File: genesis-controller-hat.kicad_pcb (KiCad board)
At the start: 2 copper layers, 65 x 56 mm, 5 parts, among them J1 GPIO, J2 DSUB-9_Socket_Horizontal_P2.7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, J3 DSUB-9_Socket_Horizontal_P2.7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

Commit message: Fix lib_footprint_mismatch -- DRC down to a single pre-existing item
J1's embedded PinSocket_2x20_P2.54mm_Vertical footprint drifted from the
system library's copy during the KiCad 9->10 upgrade (pad shape changed
from OVAL to CIRCLE -- cosmetic for a 1.7x1.7mm round pad, since equal
width/height makes the two shapes identical). Fixed the same way as the
schematic-side symbol drift: removed J1, added a fresh copy of the same
footprint straight from the system library at the same position/rotation/
flip state, and reassigned every pad's net by pad number. Verified pad
count, positions, sizes, and drills matched exactly before swapping (only
shape differed).

Side effect: unconnected_items dropped from 2 to 1. Removing J1 pruned
several stale net-table entries for GPIO pins with no real circuit (I2C,
UART, I2S, EEPROM ID -- already inert, unreferenced by any track), which
happened to include the "J1 pins 2/4 unused +5V" pair. The remaining
+3.3V pins 1/17 item is unrelated and not fixable without a pointless
jumper (they're already tied together upstream on the Pi).

DRC: 2 errors/1 warning -> 1 error/0 warnings. ERC remains 0/0.
check_pinmap.py and a top+bottom render confirm nothing else moved.

Co-Authored-By: Claude Sonnet 5 <noreply@anthropic.com>
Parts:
- J1: value GPIO -> PinSocket_2x20_P2.54mm_Vertical; footprint Connector_PinSocket_2.54mm:PinSocket_2x20_P2.54mm_Vertical -> PinSocket_2x20_P2.54mm_Vertical
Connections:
- J1 pad 10: /GPIO15/RXD0 -> (no net)
- J1 pad 12: /GPIO18/PCM.CLK -> (no net)
- J1 pad 2: +5V -> (no net)
- J1 pad 21: /GPIO9/SPI0.MISO -> (no net)
- J1 pad 22: /GPIO25 -> (no net)
- J1 pad 23: /GPIO11/SPI0.SCLK -> (no net)
- J1 pad 24: /GPIO8/SPI0.CE0 -> (no net)
- J1 pad 27: /ID_SDA -> (no net)
- J1 pad 28: /ID_SCL -> (no net)
- J1 pad 3: /GPIO2/SDA1 -> (no net)
- J1 pad 35: /GPIO19/PCM.FS -> (no net)
- J1 pad 38: /GPIO20/PCM.DIN -> (no net)
- J1 pad 4: +5V -> (no net)
- J1 pad 40: /GPIO21/PCM.DOUT -> (no net)
- J1 pad 5: /GPIO3/SCL1 -> (no net)
- J1 pad 8: /GPIO14/TXD0 -> (no net)

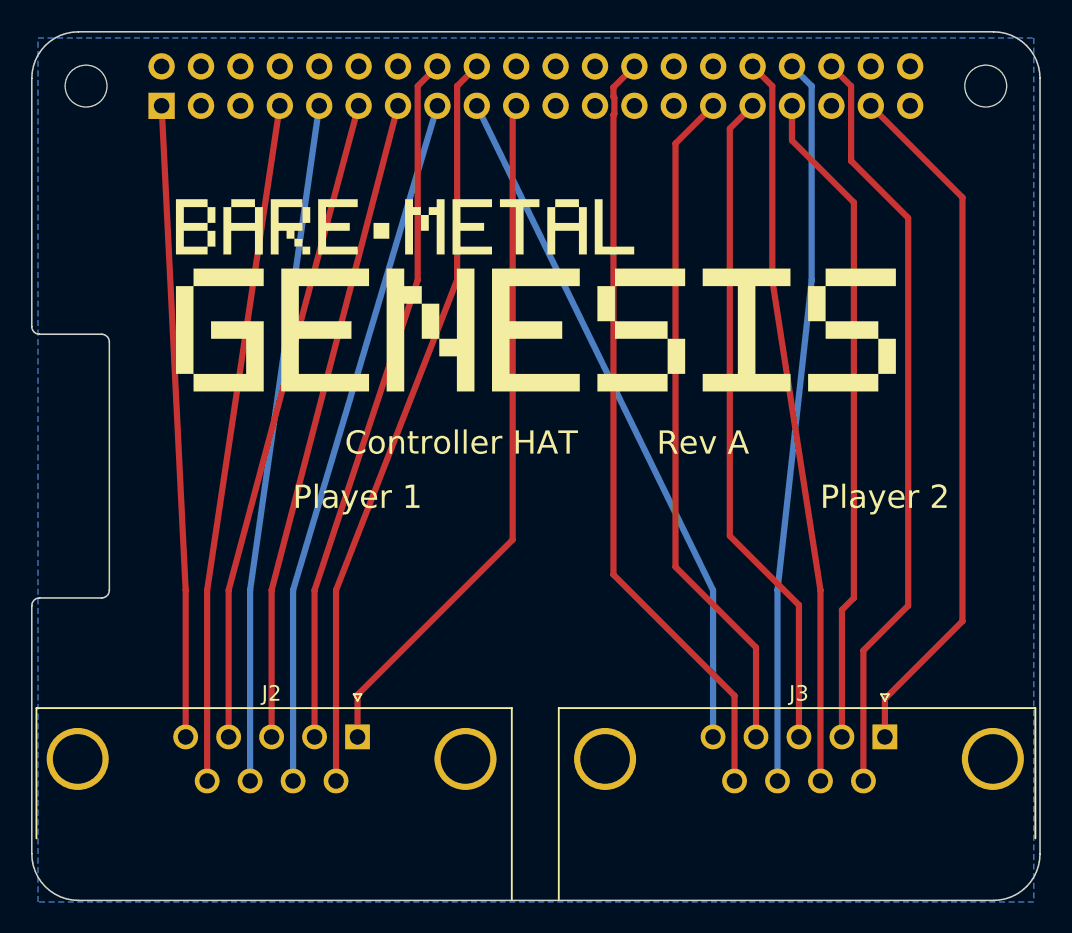
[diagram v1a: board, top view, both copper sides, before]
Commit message: Correct J2/J3 from female DB9 sockets to male DB9 pins
A real Sega Genesis controller's cable ends in a female DB9 connector, so
the HAT needs male ports to receive it -- the opposite of what had been
designed. This was never checked against a datasheet, photo, or real
hardware until physically verified against two real controllers (original
and third-party). Corrected schematic symbols (DE9_Socket_MountingHoles ->
DE9_Pins_MountingHoles) and PCB footprints (DSUB-9_Socket_Horizontal_... ->
DSUB-9_Pins_Horizontal_..., same overhang/mounting-hole variant).

A male DB9's physical pin order mirrors a female one's left-to-right, which
broke the earlier GPIO reassignment's careful non-crossing correspondence
(verified: the resulting conflict graph had 65 edges and wasn't
2-colorable). Re-derived a new GPIO assignment matched to the male
connector's actual pin order (see
docs/reviews/2026-07-22-pinmap-reassignment.md for the full analysis);
GPIO12/23 move to spare, GPIO9/11 move out of spare. Verified zero
crossings computationally before implementing.

J2/J3 re-placed (mounting holes also mirror position) and fully re-routed,
including activating J1's previously-unwired GPIO9/GPIO11 pins and freeing
GPIO12/GPIO23. scripts/check_pinmap.py updated for the mirrored pin
offsets. Final state: ERC 0/0, DRC 4 errors/0 warnings (only +3V3's
structurally-unavoidable long diagonal remains, down from 26 crossings in
the first routing attempt after the gender fix).

Co-Authored-By: Claude Sonnet 5 <noreply@anthropic.com>
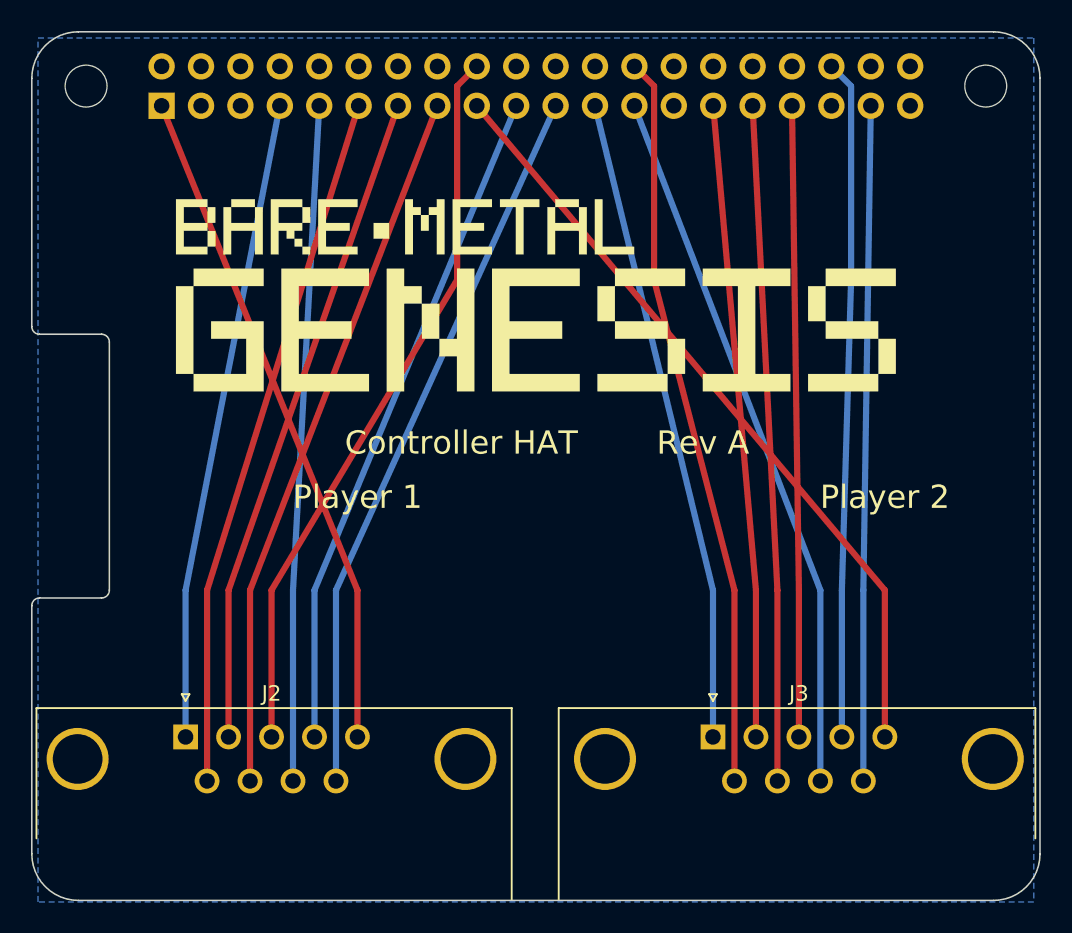
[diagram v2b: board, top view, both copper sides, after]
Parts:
- J2, J3: value DSUB-9_Socket_Horizontal_P2.77x2.84mm_EdgePinOffset7.70mm_Housed_MountingHolesOffset9.12mm -> DSUB-9_Pins_Horizontal_P2.77x2.84mm_EdgePinOffset7.70mm_Housed_MountingHolesOffset9.12mm; footprint DSUB-9_Socket_Horizontal_P2.77x2.84mm_EdgePinOffset7.70mm_Housed_MountingHolesOffset9.12mm -> DSUB-9_Pins_Horizontal_P2.77x2.84mm_EdgePinOffset7.70mm_Housed_MountingHolesOffset9.12mm
- moved J3 11.1 mm to (143.9, 89.5)
- moved J2 11.1 mm to (109.9, 89.5)
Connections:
- J1 pad 16: /GPIO23 -> (no net)
- J1 pad 21: (no net) -> /GPIO9/SPI0.MISO
- J1 pad 23: (no net) -> /GPIO11/SPI0.SCLK
- J1 pad 32: /GPIO12/PWM0 -> (no net)
- J2 pad 1: /GPIO10/SPI0.MOSI -> /GPIO4/GPCLK0
- J2 pad 2: /GPIO23 -> /GPIO27
- J2 pad 3: /GPIO27 -> /GPIO24
- J2 pad 4: /GPIO17 -> /GPIO10/SPI0.MOSI
- J2 pad 6: /GPIO24 -> /GPIO17
- J2 pad 9: /GPIO4/GPCLK0 -> /GPIO9/SPI0.MISO
- J3 pad 1: /GPIO26 -> /GPIO11/SPI0.SCLK
- J3 pad 2: /GPIO13/PWM1 -> /GPIO5
- J3 pad 3: /GPIO6 -> /GPIO13/PWM1
- J3 pad 4: /GPIO5 -> /GPIO16
- J3 pad 6: /GPIO16 -> /GPIO7/SPI0.CE1
- J3 pad 7: /GPIO12/PWM0 -> /GPIO6
- J3 pad 9: /GPIO7/SPI0.CE1 -> /GPIO26
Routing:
- net /GPIO12/PWM0: track 46.8 -> 0.00 mm
- net /GPIO9/SPI0.MISO: track 0.00 -> 46.6 mm
- net /GPIO23: track 44.8 -> 0.00 mm
- net /GPIO11/SPI0.SCLK: track 0.00 -> 41.6 mm
- net +3V3: track 84.9 -> 93.4 mm
- net /GPIO16: track 49.3 -> 43.8 mm
- net /GPIO17: track 41.8 -> 45.0 mm
- net /GPIO5: track 43.8 -> 40.8 mm
- net /GPIO7/SPI0.CE1: track 49.9 -> 47.3 mm
- net /GPIO4/GPCLK0: track 43.9 -> 41.3 mm
- net /GPIO13/PWM1: track 42.7 -> 40.7 mm
- net /GPIO26: track 45.2 -> 43.5 mm
- net /GPIO10/SPI0.MOSI: track 44.9 -> 43.3 mm
- net GND: track 90.6 -> 89.3 mm
- net /GPIO24: track 48.1 -> 47.1 mm
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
